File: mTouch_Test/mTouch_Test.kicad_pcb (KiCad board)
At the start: 2 copper layers, 91 parts, among them J401 USB_B_Micro, J501 Prog, J601 Barrel_Jack_Switch, Q501 BSS214NW, Q601 Si2319CDS, U201 PIC18LF67K40-I_PT, U301 ISO7331C, U401 74LVC1G17, U402 FT234XD, U403 TPD3S014DBVR, U501 TL331, U502 74LVC1G86, U601 MCP1700-3302E

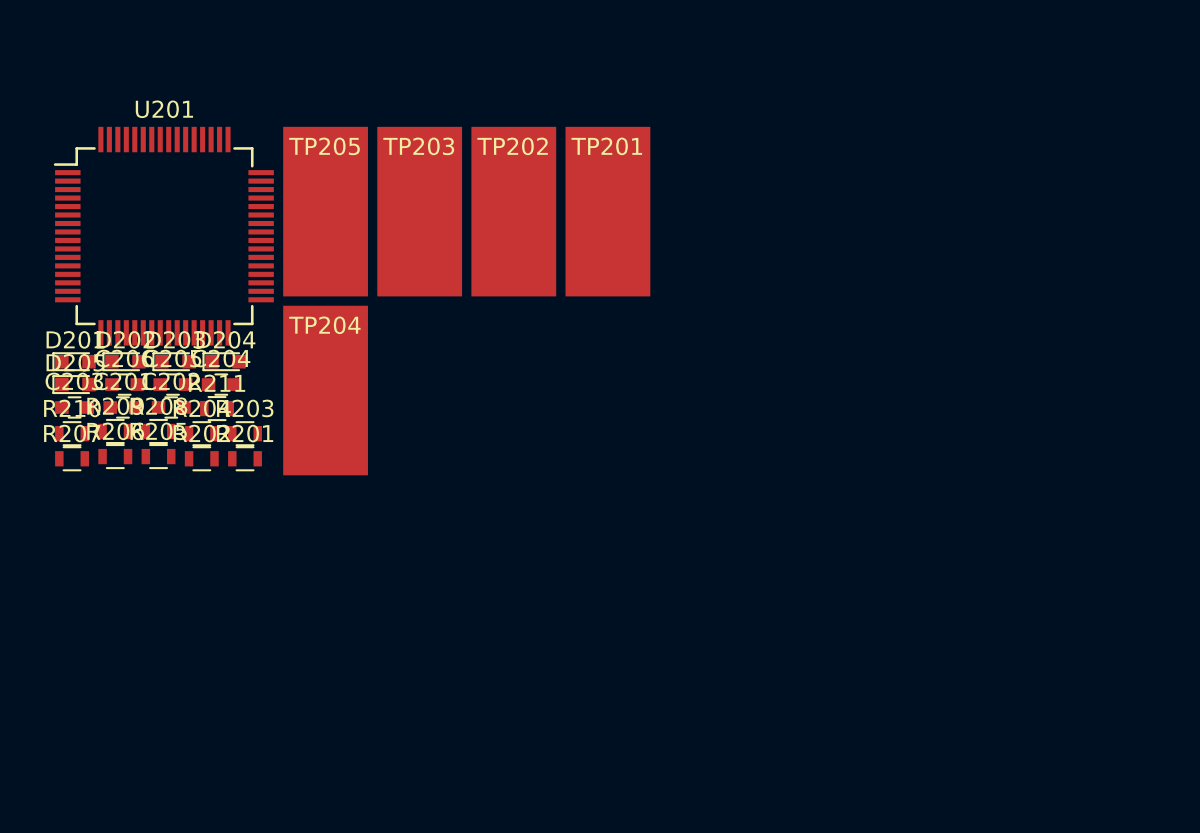
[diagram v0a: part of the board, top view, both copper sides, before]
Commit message: Arranged micro
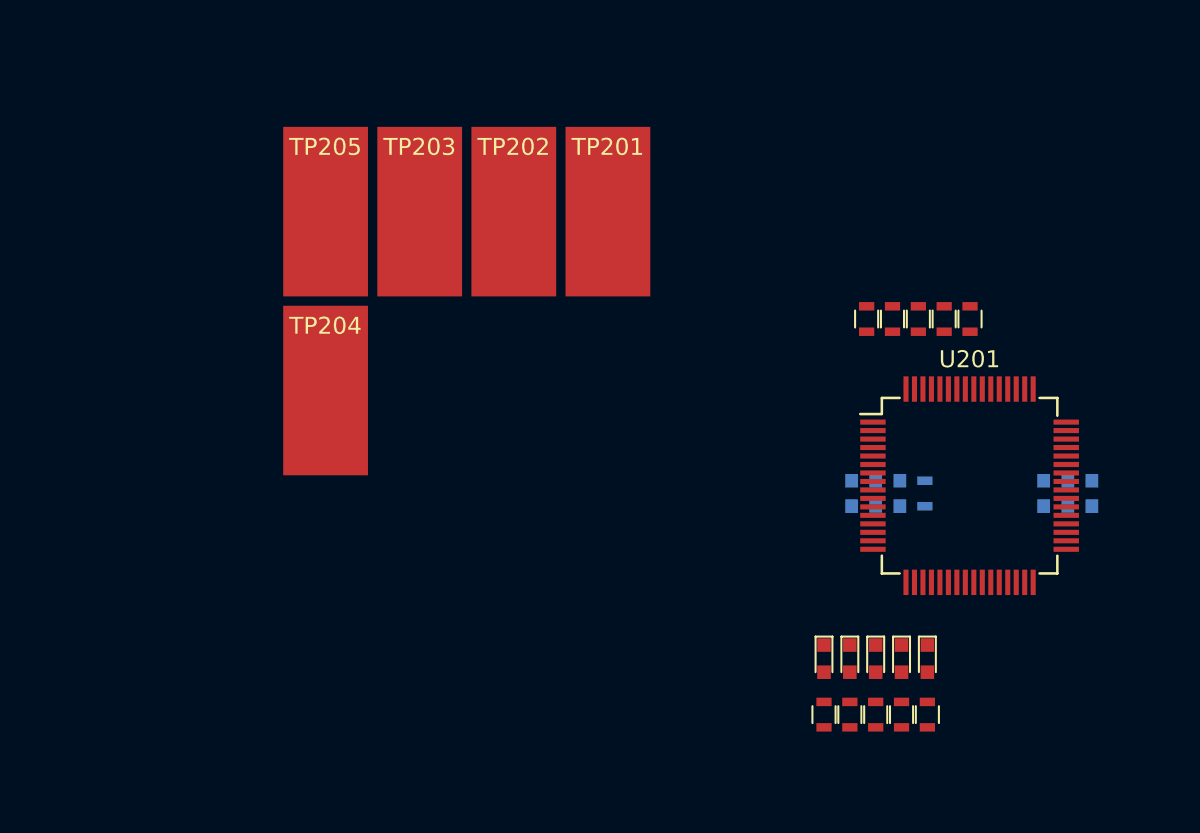
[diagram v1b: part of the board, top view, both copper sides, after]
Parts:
- C201, C202, C203, C204, C205, C206, R201: moved to B.Cu
- moved C203 57.4 mm to (93.5, 43.0), turned to 90 degrees
- moved C201 57.4 mm to (96.3, 43.0), turned to 90 degrees
- moved D201 53.2 mm to (86.6, 52.8), turned to 270 degrees
- moved C202 53.1 mm to (94.9, 43.0), turned to 90 degrees
- moved R207 52.6 mm to (86.6, 56.1), turned to 90 degrees
- moved R206 51.1 mm to (89.1, 32.7), turned to 90 degrees
- moved U201 49.7 mm to (89.1, 42.6)
- moved D202 49.0 mm to (85.1, 52.8), turned to 270 degrees
- moved R210 48.8 mm to (82.0, 56.1), turned to 90 degrees
- moved R209 47.8 mm to (83.6, 56.1), turned to 90 degrees
- moved R205 47.0 mm to (87.6, 32.7), turned to 90 degrees
- moved D205 47.0 mm to (80.5, 52.8), turned to 270 degrees
- moved R208 46.9 mm to (85.1, 56.1), turned to 90 degrees
- moved D203 44.9 mm to (83.6, 52.8), turned to 270 degrees
- moved C206 43.3 mm to (82.1, 43.0), turned to 90 degrees
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
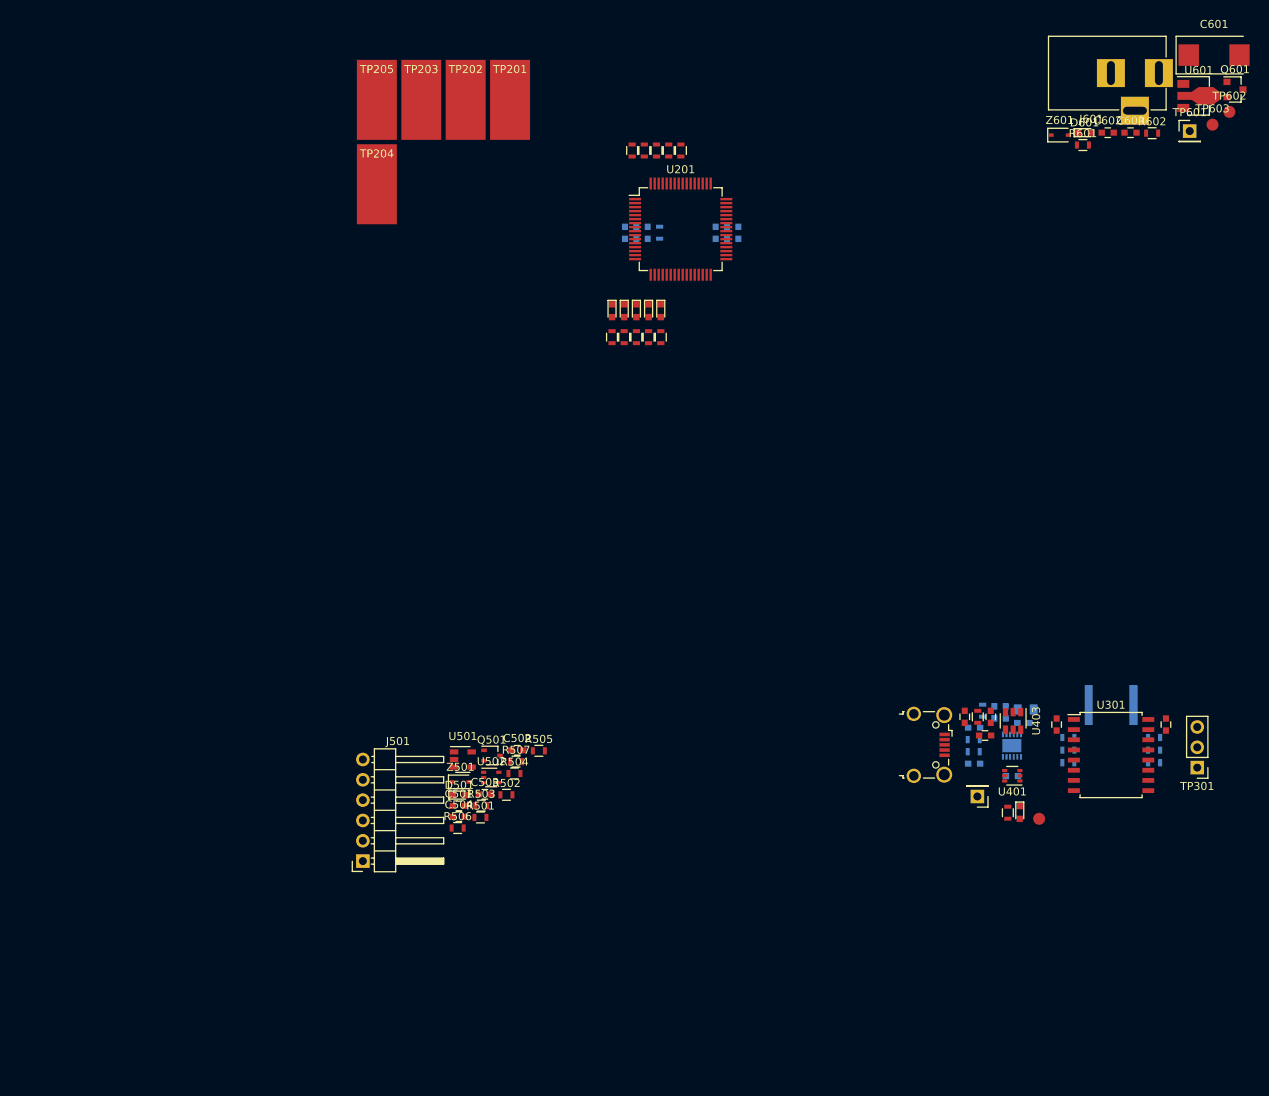
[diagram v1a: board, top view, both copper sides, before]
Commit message: Arranged programing detection circuits
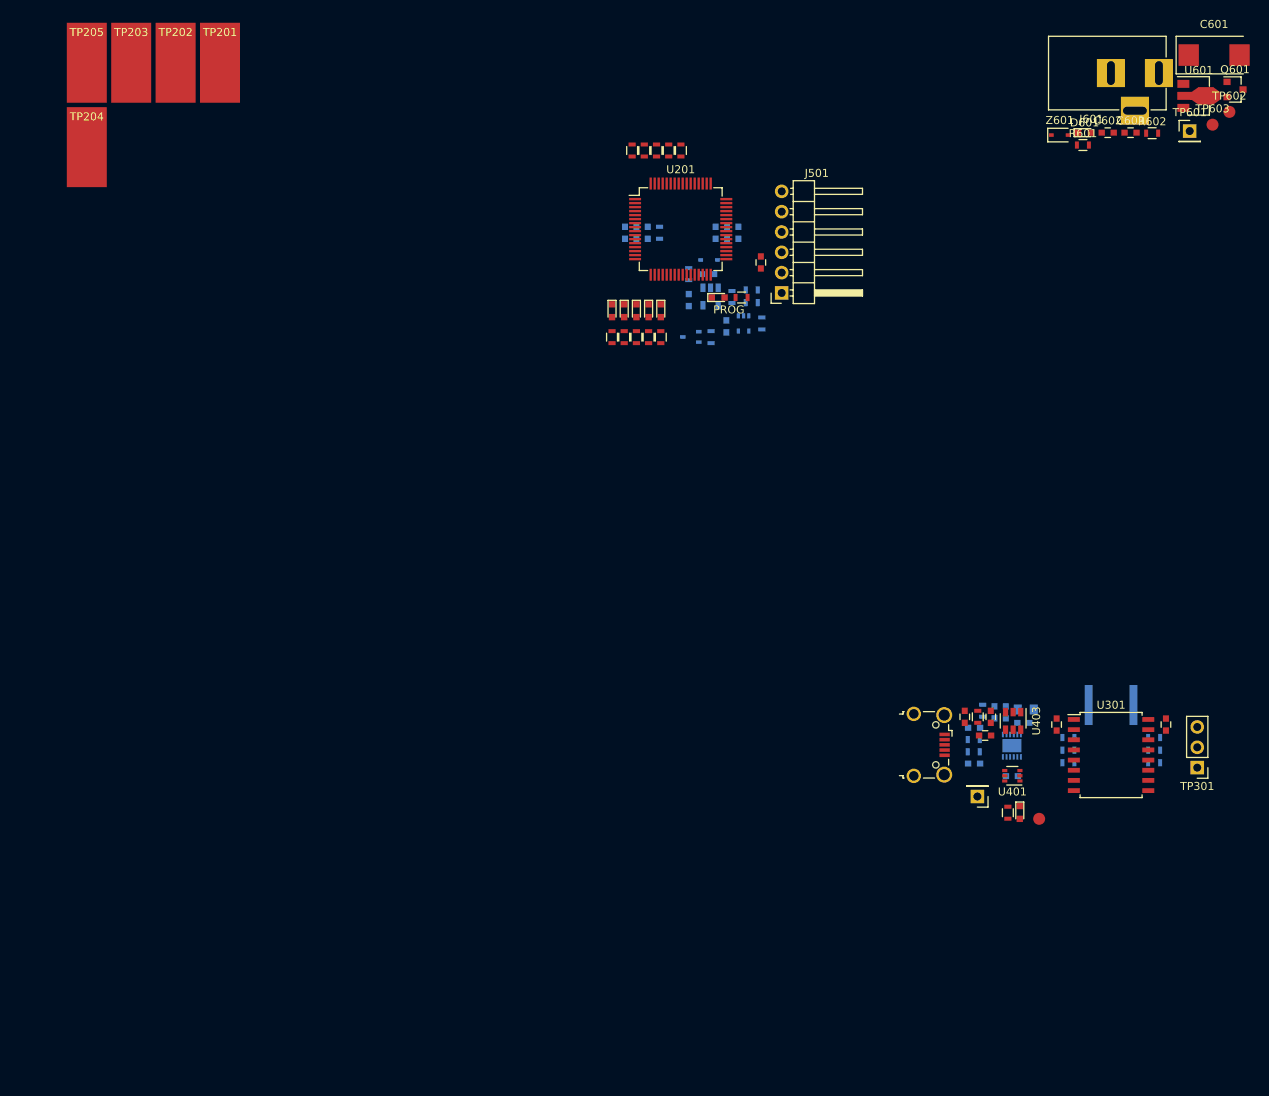
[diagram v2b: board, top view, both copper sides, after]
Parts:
- C501, C502, C503, Q501, R501, R502, R503, R504, R505, R506, U501, U502, Z501: moved to B.Cu
- moved J501 88.2 mm to (101.7, 37.8)
- moved C504 78.9 mm to (99.1, 46.7), turned to 90 degrees
- moved C501 73.4 mm to (92.5, 48.2)
- moved R503 72.8 mm to (98.0, 50.2), turned to 180 degrees
- moved R501 72.7 mm to (90.1, 48.2), turned to 90 degrees
- moved Z501 72.3 mm to (92.6, 46.4)
- moved D501 70.1 mm to (93.8, 51.1)
- moved R506 69.1 mm to (92.9, 56.1), turned to 270 degrees
- moved R502 68.3 mm to (95.5, 51.1), turned to 270 degrees
- moved R504 65.9 mm to (98.0, 51.8)
- moved C503 65.8 mm to (94.8, 54.7), turned to 90 degrees
- moved U501 65.6 mm to (92.8, 51.0), turned to 270 degrees
- moved U502 64.9 mm to (97.0, 54.4), turned to 270 degrees
- moved R507 64.5 mm to (96.7, 51.1), turned to 180 degrees
- moved R505 60.3 mm to (99.3, 54.4), turned to 90 degrees
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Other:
- board text added: "PROG"

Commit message: Finished fisrt pass of arranging parts
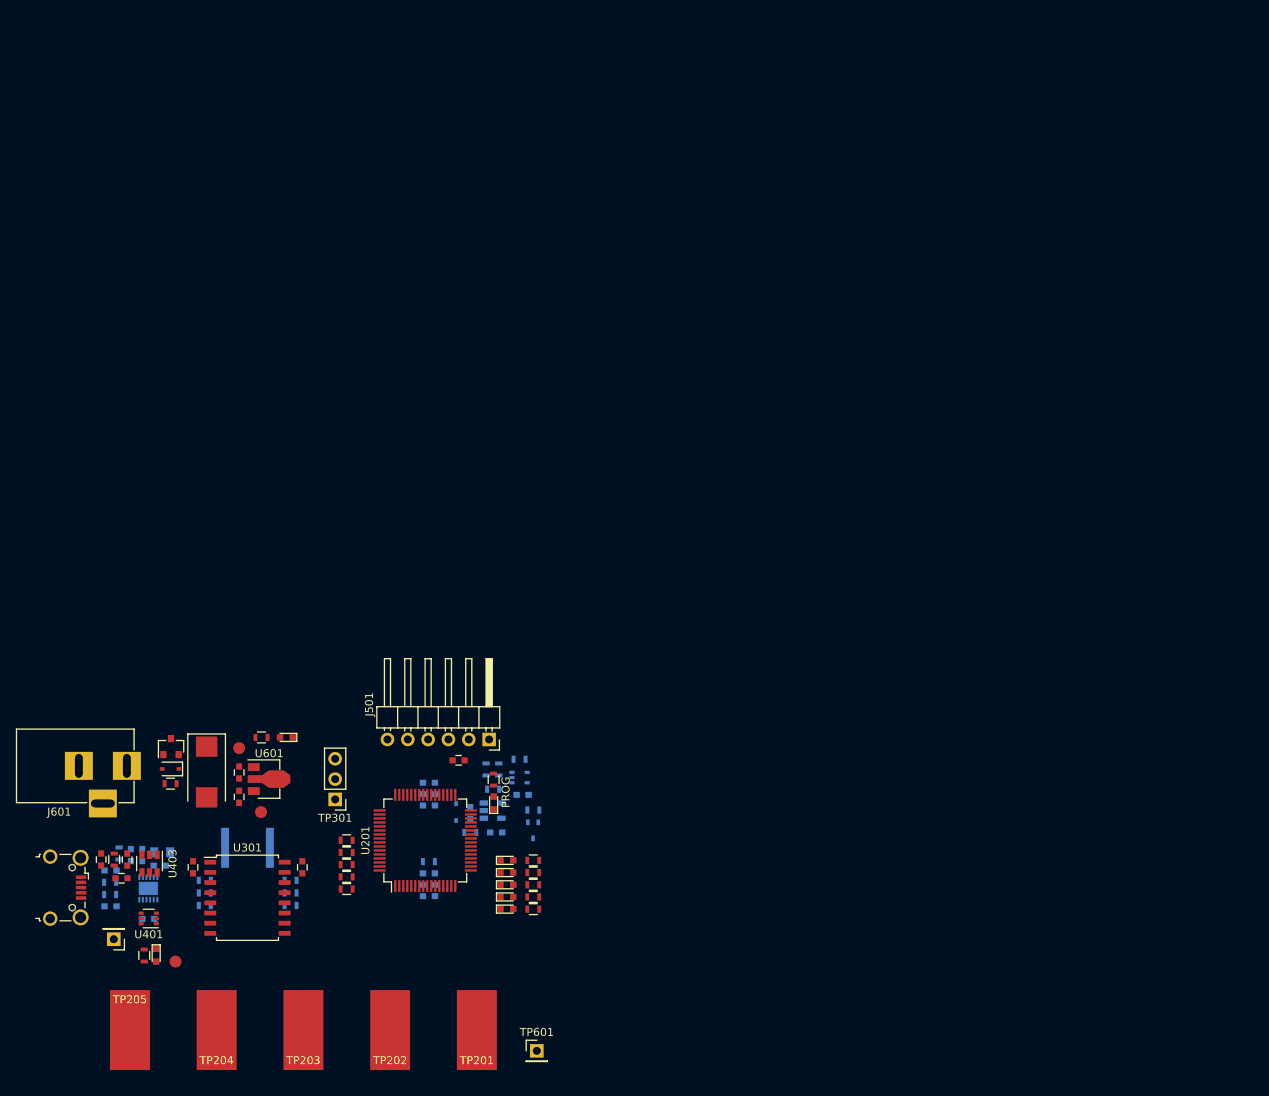
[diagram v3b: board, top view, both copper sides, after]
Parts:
- moved Q601 156.3 mm to (25.4, 107.3), turned to 90 degrees
- moved J601 155.4 mm to (19.9, 109.7)
- moved C601 154.6 mm to (29.8, 110.4), turned to 270 degrees
- moved TP602 147.1 mm to (33.9, 107.4)
- moved TP603 146.7 mm to (36.6, 115.4)
- moved U601 144.2 mm to (37.2, 111.3)
- moved TP601 141.0 mm to (71.1, 145.3)
- moved R601 139.2 mm to (25.3, 111.9)
- moved C603 139.0 mm to (33.9, 113.5), turned to 270 degrees
- moved Z601 136.5 mm to (25.3, 110.0), turned to 180 degrees
- moved C602 134.8 mm to (33.9, 110.5), turned to 90 degrees
- moved R602 134.5 mm to (36.7, 106.1)
- moved D601 125.2 mm to (39.8, 106.1), turned to 180 degrees
- moved TP201 125.1 mm to (63.6, 142.7), turned to 180 degrees
- moved TP202 123.9 mm to (52.8, 142.7), turned to 180 degrees
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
